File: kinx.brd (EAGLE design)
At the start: 122 x 86 mm, 45 parts, among them T1 MCP1825S

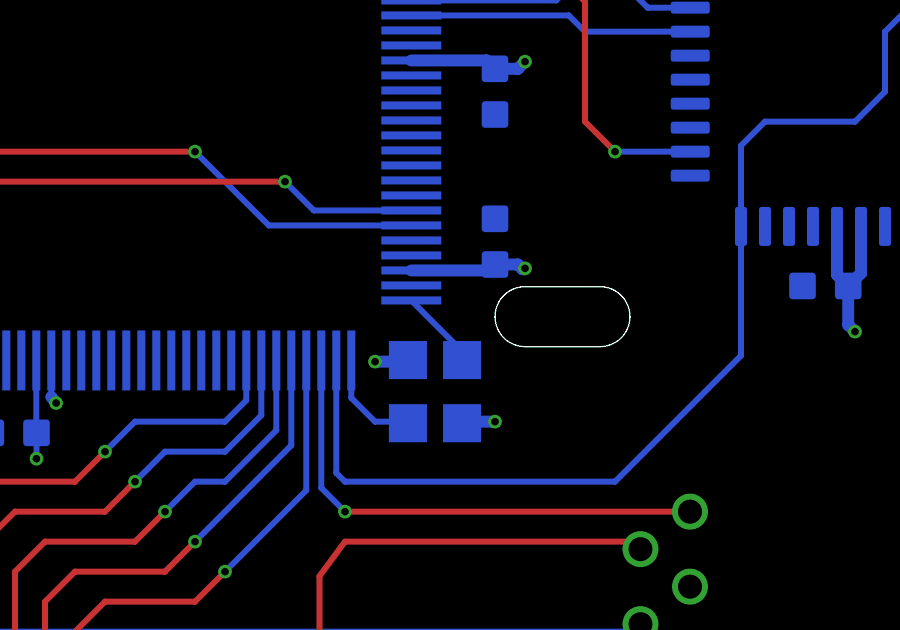
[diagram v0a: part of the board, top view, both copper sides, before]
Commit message: Move vias for easier soldering
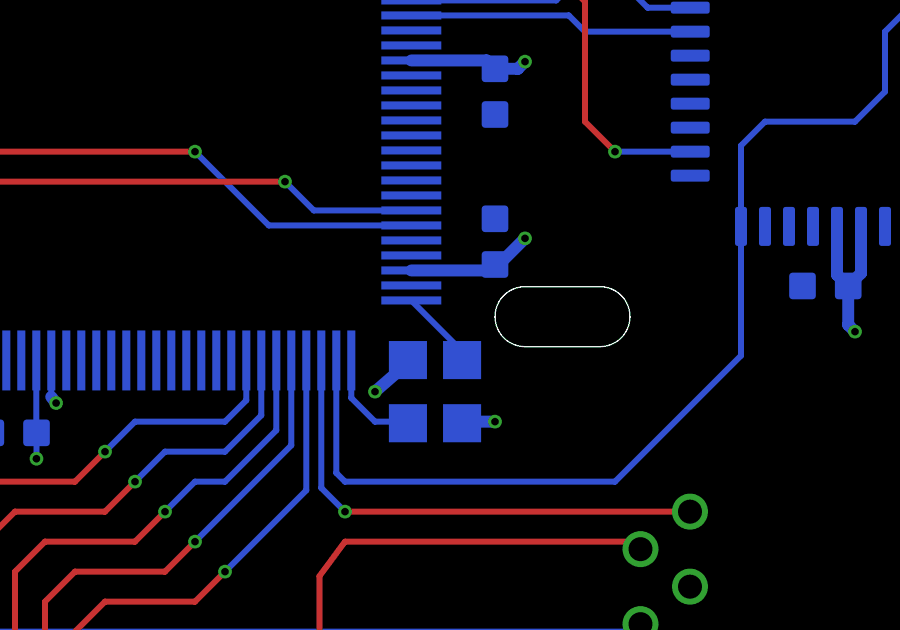
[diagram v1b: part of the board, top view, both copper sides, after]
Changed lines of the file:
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@@
 <contactref element="C13" pad="2"/>
 <wire x1="96.098" y1="38.052" x2="96.15" y2="38" width="0.4" layer="16"/>
-<wire x1="96.15" y1="38" x2="95" y2="38" width="0.4" layer="16"/>
-<via x="95" y="38" extent="1-16" drill="0.254"/>
+<wire x1="96.15" y1="38" x2="95" y2="37" width="0.4" layer="16"/>
+<via x="95" y="37" extent="1-16" drill="0.254"/>
 <wire x1="97.902" y1="35.948" x2="97.85" y2="36" width="0.4" layer="16"/>
 <wire x1="97.85" y1="36" x2="99" y2="36" width="0.4" layer="16"/>
@@
 <via x="83.715" y="34.764" extent="1-16" drill="0.254"/>
 <wire x1="96.21" y1="41.04" x2="98.802" y2="41.04" width="0.4" layer="16"/>
-<wire x1="98.802" y1="41.04" x2="99" y2="41.238" width="0.4" layer="16"/>
-<wire x1="99" y1="41.238" x2="99.762" y2="41.238" width="0.4" layer="16"/>
-<wire x1="99.762" y1="41.238" x2="99.919" y2="41.081" width="0.4" layer="16"/>
-<wire x1="99.919" y1="41.081" x2="99.9714" y2="41.081" width="0.4" layer="16"/>
-<wire x1="99.9714" y1="41.081" x2="100" y2="41.1096" width="0.4" layer="16"/>
-<via x="100" y="41.1096" extent="1-16" drill="0.254"/>
+<wire x1="99" y1="41.238" x2="98.802" y2="41.04" width="0.4" layer="16"/>
+<via x="100" y="42.1096" extent="1-16" drill="0.254"/>
 <wire x1="96.21" y1="48.04" x2="98.722" y2="48.04" width="0.4" layer="16"/>
 <wire x1="98.722" y1="48.04" x2="99" y2="47.762" width="0.4" layer="16"/>
@@
 <wire x1="87.618" y1="61.323" x2="87.614" y2="61.319" width="0.2" layer="16"/>
 <via x="87.614" y="61.319" extent="1-16" drill="0.254"/>
+<wire x1="100" y1="42.1096" x2="99.1284" y2="41.238" width="0.4" layer="16"/>
+<wire x1="99.1284" y1="41.238" x2="99" y2="41.238" width="0.4" layer="16"/>
+<wire x1="92.21" y1="59.54" x2="91.71" y2="59.54" width="0" layer="19" extent="16-16"/>
+<wire x1="87.614" y1="61.319" x2="91.71" y2="59.54" width="0" layer="19" extent="16-16"/>
+<wire x1="84.21" y1="59.54" x2="86.71" y2="59.54" width="0" layer="19" extent="16-16"/>
+<wire x1="96.21" y1="55.04" x2="92.5" y2="58" width="0" layer="19" extent="16-16"/>
+<wire x1="79" y1="63" x2="83.762" y2="62.762" width="0" layer="19" extent="16-16"/>
+<wire x1="100" y1="48" x2="100" y2="54" width="0" layer="19" extent="1-1"/>
+<wire x1="100" y1="42.1096" x2="99.762" y2="47.762" width="0" layer="19" extent="16-16"/>
+<wire x1="74.71" y1="53.04" x2="78.71" y2="59.54" width="0" layer="19" extent="16-16"/>
+<wire x1="74.71" y1="46.54" x2="74.71" y2="53.04" width="0" layer="19" extent="16-16"/>
+<wire x1="76.71" y1="38.04" x2="76.2" y2="46.3" width="0" layer="19" extent="16-16"/>
+<wire x1="83.71" y1="38.04" x2="76.71" y2="38.04" width="0" layer="19" extent="16-16"/>
+<wire x1="110.4" y1="42.5074" x2="100" y2="42.1096" width="0" layer="19" extent="16-16"/>
+<wire x1="88.81" y1="16.27" x2="83.715" y2="34.764" width="0" layer="19" extent="16-16"/>
+<wire x1="79" y1="4" x2="88.81" y2="16.27" width="0" layer="19" extent="1-1"/>
+<wire x1="69" y1="4" x2="77.75" y2="4" width="0" layer="19" extent="1-1"/>
+<wire x1="59" y1="4" x2="67.75" y2="4" width="0" layer="19" extent="1-1"/>
+<wire x1="49" y1="4" x2="57.75" y2="4" width="0" layer="19" extent="1-1"/>
+<wire x1="49" y1="73" x2="67.769" y2="53.673" width="0" layer="19" extent="16-16"/>
 </signal>
 <signal name="N$1">

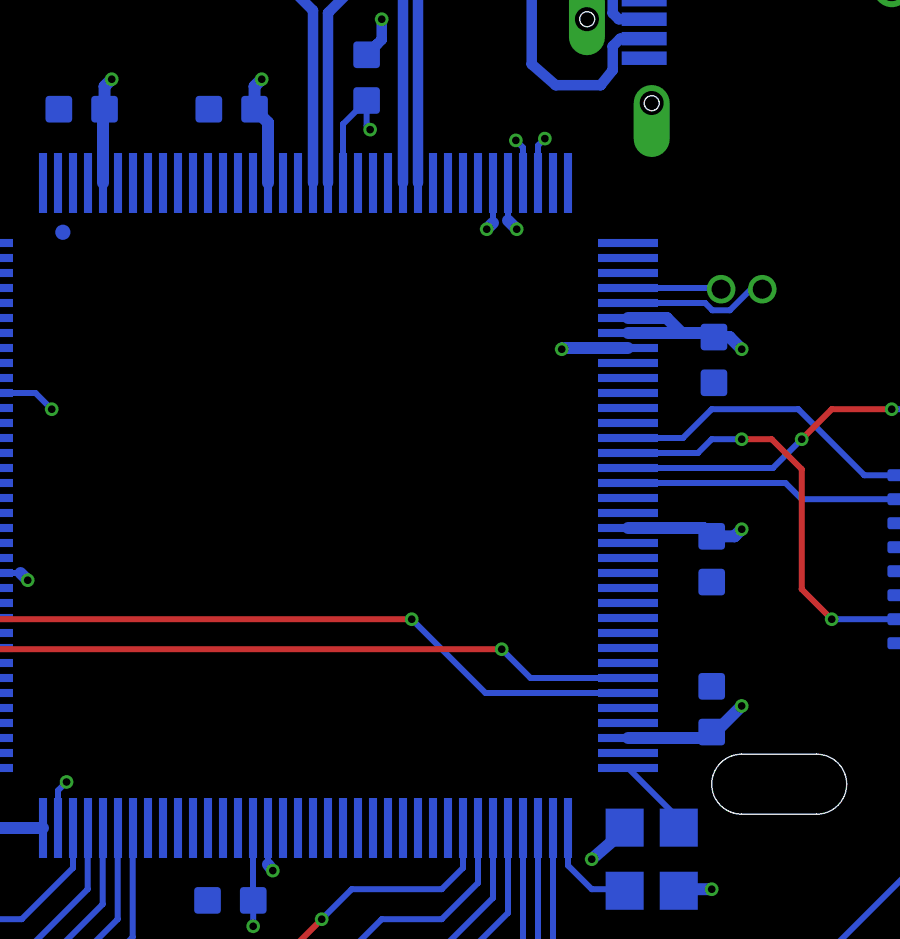
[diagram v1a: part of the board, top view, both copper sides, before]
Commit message: Connect remaining VSS pins
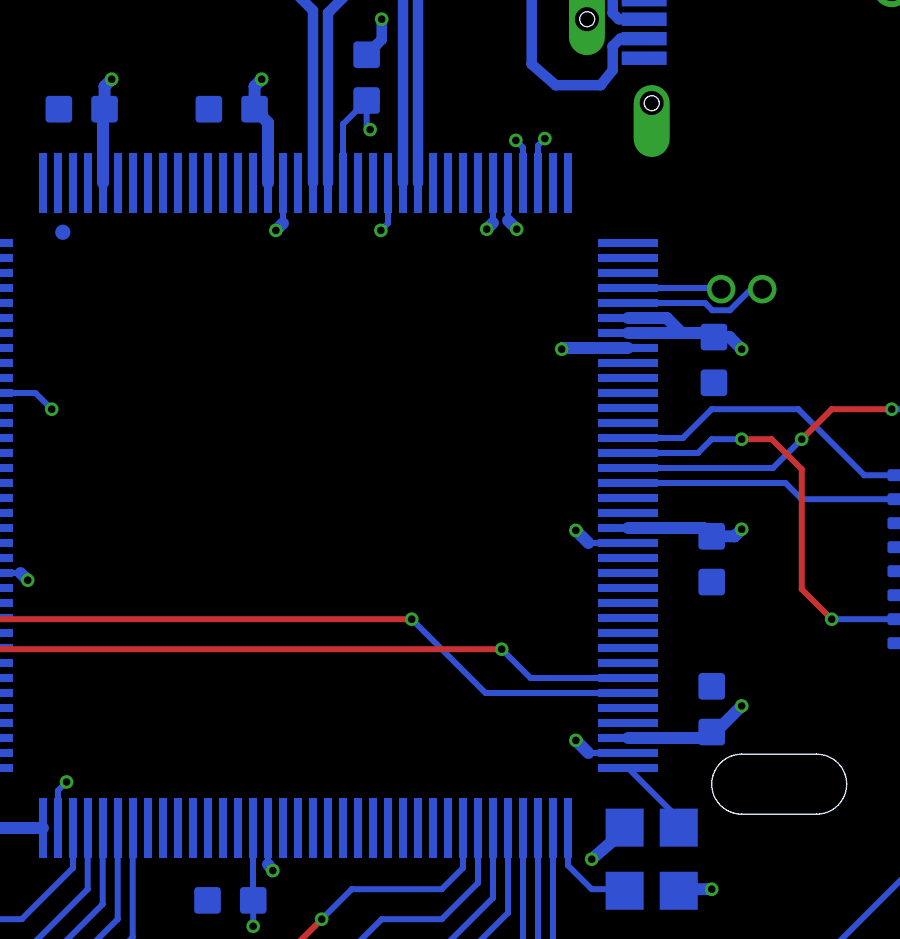
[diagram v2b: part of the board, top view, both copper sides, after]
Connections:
- removed net USB1_VSS: U$1.24
- removed net VSS: U$1.18
- net GND: now also U$1.18, U$1.24
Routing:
- net GND: track 20.3 -> 27.4 mm, vias 35 -> 39
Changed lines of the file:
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@@
 <wire x1="98.812" y1="66.3" x2="96.75" y2="66.3" width="0.35" layer="16"/>
 <wire x1="98.812" y1="66.3" x2="99.472" y2="66.96" width="0.35" layer="16"/>
+<contactref element="U$1" pad="18"/>
+<contactref element="U$1" pad="24"/>
+<via x="84.472" y="57.96" extent="1-16" drill="0.254"/>
+<wire x1="84.71" y1="59.54" x2="84.71" y2="58.198" width="0.2" layer="16"/>
+<wire x1="84.71" y1="58.198" x2="84.472" y2="57.96" width="0.4" layer="16"/>
+<via x="94.472" y="47.96" extent="1-16" drill="0.254"/>
+<via x="94.472" y="40.96" extent="1-16" drill="0.254"/>
+<wire x1="96.21" y1="40.54" x2="94.892" y2="40.54" width="0.2" layer="16"/>
+<wire x1="94.892" y1="40.54" x2="94.472" y2="40.96" width="0.4" layer="16"/>
+<wire x1="96.21" y1="47.54" x2="94.892" y2="47.54" width="0.2" layer="16"/>
+<wire x1="94.892" y1="47.54" x2="94.472" y2="47.96" width="0.4" layer="16"/>
+<via x="87.972" y="57.96" extent="1-16" drill="0.254"/>
+<wire x1="88.21" y1="59.54" x2="88.21" y2="58.198" width="0.2" layer="16"/>
+<wire x1="88.21" y1="58.198" x2="87.972" y2="57.96" width="0.2" layer="16"/>
+<wire x1="120" y1="73" x2="120" y2="84" width="0" layer="19" extent="1-1"/>
+<wire x1="108" y1="84" x2="120" y2="84" width="0" layer="19" extent="1-1"/>
+<wire x1="120" y1="61" x2="120" y2="73" width="0" layer="19" extent="1-1"/>
+<wire x1="113.2606" y1="60.2512" x2="120" y2="61" width="0" layer="19" extent="1-1"/>
+<wire x1="113.2606" y1="53.7488" x2="113.2606" y2="60.2512" width="0" layer="19" extent="1-1"/>
+<wire x1="120" y1="49" x2="113.2606" y2="53.7488" width="0" layer="19" extent="1-1"/>
+<wire x1="120" y1="38" x2="120" y2="49" width="0" layer="19" extent="1-1"/>
+<wire x1="109.25" y1="40.523" x2="120" y2="38" width="0" layer="19" extent="16-16"/>
+<wire x1="109.6" y1="42.5074" x2="109.25" y2="40.523" width="0" layer="19" extent="16-16"/>
+<wire x1="108.8" y1="42.5074" x2="109.6" y2="42.5074" width="0" layer="19" extent="16-16"/>
+<wire x1="99" y1="42.762" x2="108.8" y2="42.5074" width="0" layer="19" extent="16-16"/>
+<wire x1="99" y1="46.238" x2="99" y2="42.762" width="0" layer="19" extent="16-16"/>
+<wire x1="96.21" y1="47.54" x2="99" y2="46.238" width="0" layer="19" extent="16-16"/>
+<wire x1="96.21" y1="40.54" x2="99" y2="42.762" width="0" layer="19" extent="16-16"/>
+<wire x1="96.098" y1="38.052" x2="96.21" y2="40.54" width="0" layer="19" extent="16-16"/>
+<wire x1="97.85" y1="36" x2="96.15" y2="38" width="0" layer="19" extent="16-16"/>
+<wire x1="99.075" y1="52.881" x2="96.21" y2="47.54" width="0" layer="19" extent="16-16"/>
+<wire x1="96.96" y1="54.04" x2="99.075" y2="52.881" width="0" layer="19" extent="16-16"/>
+<wire x1="93.21" y1="59.54" x2="94.04" y2="54.04" width="0" layer="19" extent="16-16"/>
+<wire x1="92.71" y1="59.54" x2="93.21" y2="59.54" width="0" layer="19" extent="16-16"/>
+<wire x1="97" y1="62.206" x2="93.439" y2="61.021" width="0" layer="19" extent="1-1"/>
+<wire x1="94.841" y1="65" x2="97" y2="62.206" width="0" layer="19" extent="1-1"/>
+<wire x1="96.75" y1="66.3" x2="94.841" y2="65" width="0" layer="19" extent="16-16"/>
+<wire x1="97" y1="67.794" x2="96.75" y2="66.3" width="0" layer="19" extent="16-16"/>
+<wire x1="88.21" y1="59.54" x2="92.472" y2="60.96" width="0" layer="19" extent="16-16"/>
+<wire x1="85.21" y1="59.54" x2="88.21" y2="59.54" width="0" layer="19" extent="16-16"/>
+<wire x1="84.71" y1="59.54" x2="85.21" y2="59.54" width="0" layer="19" extent="16-16"/>
+<wire x1="82.238" y1="62" x2="84.71" y2="59.54" width="0" layer="19" extent="16-16"/>
+<wire x1="79.21" y1="59.54" x2="82.238" y2="62" width="0" layer="19" extent="16-16"/>
+<wire x1="77.238" y1="62" x2="79.21" y2="59.54" width="0" layer="19" extent="16-16"/>
+<wire x1="87.497" y1="63.814" x2="88.21" y2="59.54" width="0" layer="19" extent="16-16"/>
+<wire x1="76.46" y1="52.54" x2="79.21" y2="59.54" width="0" layer="19" extent="16-16"/>
+<wire x1="70.238" y1="53" x2="74.71" y2="52.54" width="0" layer="19" extent="16-16"/>
+<wire x1="74.71" y1="46.04" x2="77" y2="52" width="0" layer="19" extent="16-16"/>
+<wire x1="77.494" y1="39.574" x2="74.71" y2="46.04" width="0" layer="19" extent="16-16"/>
+<wire x1="74.793" y1="36.525" x2="77.21" y2="38.04" width="0" layer="19" extent="16-16"/>
+<wire x1="82.194" y1="35.627" x2="77.21" y2="38.04" width="0" layer="19" extent="16-16"/>
+<wire x1="84.208" y1="36.827" x2="82.194" y2="35.627" width="0" layer="19" extent="16-16"/>
+<wire x1="67.238" y1="36" x2="74.793" y2="36.525" width="0" layer="19" extent="16-16"/>
+<wire x1="96" y1="84" x2="108" y2="84" width="0" layer="19" extent="1-1"/>
+<wire x1="84" y1="84" x2="96" y2="84" width="0" layer="19" extent="1-1"/>
+<wire x1="73" y1="84" x2="84" y2="84" width="0" layer="19" extent="1-1"/>
+<wire x1="61" y1="84" x2="73" y2="84" width="0" layer="19" extent="1-1"/>
+<wire x1="120" y1="26" x2="120" y2="38" width="0" layer="19" extent="1-1"/>
+<wire x1="49" y1="84" x2="61" y2="84" width="0" layer="19" extent="1-1"/>
+<wire x1="38" y1="84" x2="49" y2="84" width="0" layer="19" extent="1-1"/>
+<wire x1="40" y1="73.175" x2="38" y2="84" width="0" layer="19" extent="16-16"/>
+<wire x1="40" y1="66.825" x2="40" y2="73.175" width="0" layer="19" extent="16-16"/>
+<wire x1="47" y1="70.984" x2="40" y2="73.175" width="0" layer="19" extent="16-16"/>
+<wire x1="32" y1="71.238" x2="40" y2="73.175" width="0" layer="19" extent="16-16"/>
+<wire x1="28.016" y1="70" x2="32" y2="71.238" width="0" layer="19" extent="16-16"/>
+<wire x1="26.5" y1="63.694" x2="28.016" y2="70" width="0" layer="19" extent="16-16"/>
+<wire x1="26.25" y1="62.2" x2="26.5" y2="63.694" width="0" layer="19" extent="16-16"/>
+<wire x1="24.341" y1="60.9" x2="26.25" y2="62.2" width="0" layer="19" extent="16-16"/>
+<wire x1="26.5" y1="58.106" x2="24.341" y2="60.9" width="0" layer="19" extent="1-1"/>
+<wire x1="120" y1="14" x2="120" y2="26" width="0" layer="19" extent="1-1"/>
+<wire x1="120" y1="2" x2="120" y2="14" width="0" layer="19" extent="1-1"/>
+<wire x1="26" y1="84" x2="38" y2="84" width="0" layer="19" extent="1-1"/>
+<wire x1="14" y1="84" x2="26" y2="84" width="0" layer="19" extent="1-1"/>
+<wire x1="2" y1="84" x2="14" y2="84" width="0" layer="19" extent="1-1"/>
+<wire x1="2" y1="73" x2="2" y2="84" width="0" layer="19" extent="1-1"/>
+<wire x1="2" y1="61" x2="2" y2="73" width="0" layer="19" extent="1-1"/>
+<wire x1="2" y1="49" x2="2" y2="61" width="0" layer="19" extent="1-1"/>
+<wire x1="2" y1="38" x2="2" y2="49" width="0" layer="19" extent="1-1"/>
+<wire x1="2" y1="26" x2="2" y2="38" width="0" layer="19" extent="1-1"/>
+<wire x1="2" y1="14" x2="2" y2="26" width="0" layer="19" extent="1-1"/>
+<wire x1="2" y1="2" x2="2" y2="14" width="0" layer="19" extent="1-1"/>
+<wire x1="51.81" y1="39.81" x2="67.238" y2="36" width="0" layer="19" extent="16-16"/>
+<wire x1="51.81" y1="32.19" x2="51.81" y2="39.81" width="0" layer="19" extent="1-1"/>
+<wire x1="88.81" y1="13.73" x2="82.194" y2="35.627" width="0" layer="19" extent="16-16"/>
+<wire x1="88.81" y1="11.19" x2="88.81" y2="13.73" width="0" layer="19" extent="1-1"/>
 </signal>
 <signal name="N$12">
@@
 <wire x1="100" y1="42.1096" x2="99.1284" y2="41.238" width="0.4" layer="16"/>
 <wire x1="99.1284" y1="41.238" x2="99" y2="41.238" width="0.4" layer="16"/>
-<wire x1="92.21" y1="59.54" x2="91.71" y2="59.54" width="0" layer="19" extent="16-16"/>
-<wire x1="87.614" y1="61.319" x2="91.71" y2="59.54" width="0" layer="19" extent="16-16"/>
-<wire x1="84.21" y1="59.54" x2="86.71" y2="59.54" width="0" layer="19" extent="16-16"/>
-<wire x1="96.21" y1="55.04" x2="92.5" y2="58" width="0" layer="19" extent="16-16"/>
-<wire x1="79" y1="63" x2="83.762" y2="62.762" width="0" layer="19" extent="16-16"/>
-<wire x1="100" y1="48" x2="100" y2="54" width="0" layer="19" extent="1-1"/>
-<wire x1="100" y1="42.1096" x2="99.762" y2="47.762" width="0" layer="19" extent="16-16"/>
-<wire x1="74.71" y1="53.04" x2="78.71" y2="59.54" width="0" layer="19" extent="16-16"/>
-<wire x1="74.71" y1="46.54" x2="74.71" y2="53.04" width="0" layer="19" extent="16-16"/>
-<wire x1="76.71" y1="38.04" x2="76.2" y2="46.3" width="0" layer="19" extent="16-16"/>
-<wire x1="83.71" y1="38.04" x2="76.71" y2="38.04" width="0" layer="19" extent="16-16"/>
-<wire x1="110.4" y1="42.5074" x2="100" y2="42.1096" width="0" layer="19" extent="16-16"/>
-<wire x1="88.81" y1="16.27" x2="83.715" y2="34.764" width="0" layer="19" extent="16-16"/>
-<wire x1="79" y1="4" x2="88.81" y2="16.27" width="0" layer="19" extent="1-1"/>
-<wire x1="69" y1="4" x2="77.75" y2="4" width="0" layer="19" extent="1-1"/>
-<wire x1="59" y1="4" x2="67.75" y2="4" width="0" layer="19" extent="1-1"/>
-<wire x1="49" y1="4" x2="57.75" y2="4" width="0" layer="19" extent="1-1"/>
-<wire x1="49" y1="73" x2="67.769" y2="53.673" width="0" layer="19" extent="16-16"/>
 </signal>
 <signal name="N$1">
@@
 <wire x1="28.127" y1="72.762" x2="27.889" y2="73" width="0.4" layer="16"/>
 </signal>
-<signal name="VSS">
-<contactref element="U$1" pad="18"/>
-</signal>
 <signal name="VREG_IN0">
 <contactref element="U$1" pad="22"/>
@@
 <contactref element="U$1" pad="23"/>
 </signal>
-<signal name="USB1_VSS">
-<contactref element="U$1" pad="24"/>
-</signal>
 <signal name="USB1_VBUS">
